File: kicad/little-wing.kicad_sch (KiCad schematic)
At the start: 132 parts, among them IC1 AP7335-WG-7, J1 nice!view, J10 rgb, J11 rows, J12 columns, J13 columns, J2 Battery, J3 trackball, J4 rotary, J5 trackball, J6 nice!view, J7 Battery, J8 rgb, J9 rows, SW1 Power, SW2 Reset, SW3 Reset, SW4 Power, U1 nice!nano v2, U2 PMW3610, U3 nice!nano v2

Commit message: Stashig the work
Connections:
- net MISO L renamed IRQ L
- net MISO R renamed IRQ R
- net MOSI L renamed SDIO L
- net MOSI R renamed SDIO R
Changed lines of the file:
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@@
 		)
 	)
-	(global_label "MISO R"
+	(global_label "IRQ R"
 		(shape input)
 		(at 35.56 121.92 180)
@@
 		)
 		(property "Intersheetrefs" "${INTERSHEET_REFS}"
-			(at 25.741 121.92 0)
+			(at 27.1319 121.92 0)
 			(effects
 				(font
@@
 		)
 	)
-	(global_label "MOSI L"
+	(global_label "SDIO L"
 		(shape input)
 		(at 36.83 69.85 180)
@@
 		)
 		(property "Intersheetrefs" "${INTERSHEET_REFS}"
-			(at 27.2529 69.85 0)
+			(at 27.4343 69.85 0)
 			(effects
 				(font
@@
 		)
 	)
-	(global_label "MOSI R"
+	(global_label "SDIO R"
 		(shape input)
 		(at 36.83 154.94 180)
@@
 		)
 		(property "Intersheetrefs" "${INTERSHEET_REFS}"
-			(at 27.011 154.94 0)
+			(at 27.1924 154.94 0)
 			(effects
 				(font
@@
 		)
 	)
-	(global_label "MOSI L"
+	(global_label "SDIO L"
 		(shape input)
 		(at 35.56 34.29 180)
@@
 		)
 		(property "Intersheetrefs" "${INTERSHEET_REFS}"
-			(at 25.9829 34.29 0)
-			(effects
-				(font
-					(size 1.27 1.27)
-				)
-				(justify right)
-				(hide yes)
-			)
-		)
-	)
-	(global_label "MISO L"
+			(at 26.1643 34.29 0)
+			(effects
+				(font
+					(size 1.27 1.27)
+				)
+				(justify right)
+				(hide yes)
+			)
+		)
+	)
+	(global_label "IRQ L"
 		(shape input)
 		(at 35.56 36.83 180)
@@
 		)
 		(property "Intersheetrefs" "${INTERSHEET_REFS}"
-			(at 25.9829 36.83 0)
+			(at 27.3738 36.83 0)
 			(effects
 				(font
@@
 		)
 	)
-	(global_label "MOSI R"
+	(global_label "SDIO R"
 		(shape input)
 		(at 67.31 152.4 180)
@@
 		)
 		(property "Intersheetrefs" "${INTERSHEET_REFS}"
-			(at 57.491 152.4 0)
+			(at 57.6724 152.4 0)
 			(effects
 				(font
@@
 		)
 	)
-	(global_label "MOSI R"
+	(global_label "SDIO R"
 		(shape input)
 		(at 35.56 119.38 180)
@@
 		)
 		(property "Intersheetrefs" "${INTERSHEET_REFS}"
-			(at 25.741 119.38 0)
+			(at 25.9224 119.38 0)
 			(effects
 				(font
@@
 		)
 	)
-	(global_label "MOSI L"
+	(global_label "SDIO L"
 		(shape input)
 		(at 62.23 64.77 180)
@@
 		)
 		(property "Intersheetrefs" "${INTERSHEET_REFS}"
-			(at 52.6529 64.77 0)
+			(at 52.8343 64.77 0)
 			(effects
 				(font
@@
 		)
 	)
-	(global_label "MISO R"
+	(global_label "IRQ R"
 		(shape input)
 		(at 36.83 160.02 180)
@@
 		)
 		(property "Intersheetrefs" "${INTERSHEET_REFS}"
-			(at 27.011 160.02 0)
+			(at 28.4019 160.02 0)
 			(effects
 				(font
@@
 		)
 	)
-	(global_label "MISO L"
+	(global_label "IRQ L"
 		(shape input)
 		(at 36.83 74.93 180)
@@
 		)
 		(property "Intersheetrefs" "${INTERSHEET_REFS}"
-			(at 27.2529 74.93 0)
-			(effects
-				(font
+			(at 28.6438 74.93 0)
+			(effects
+				(font

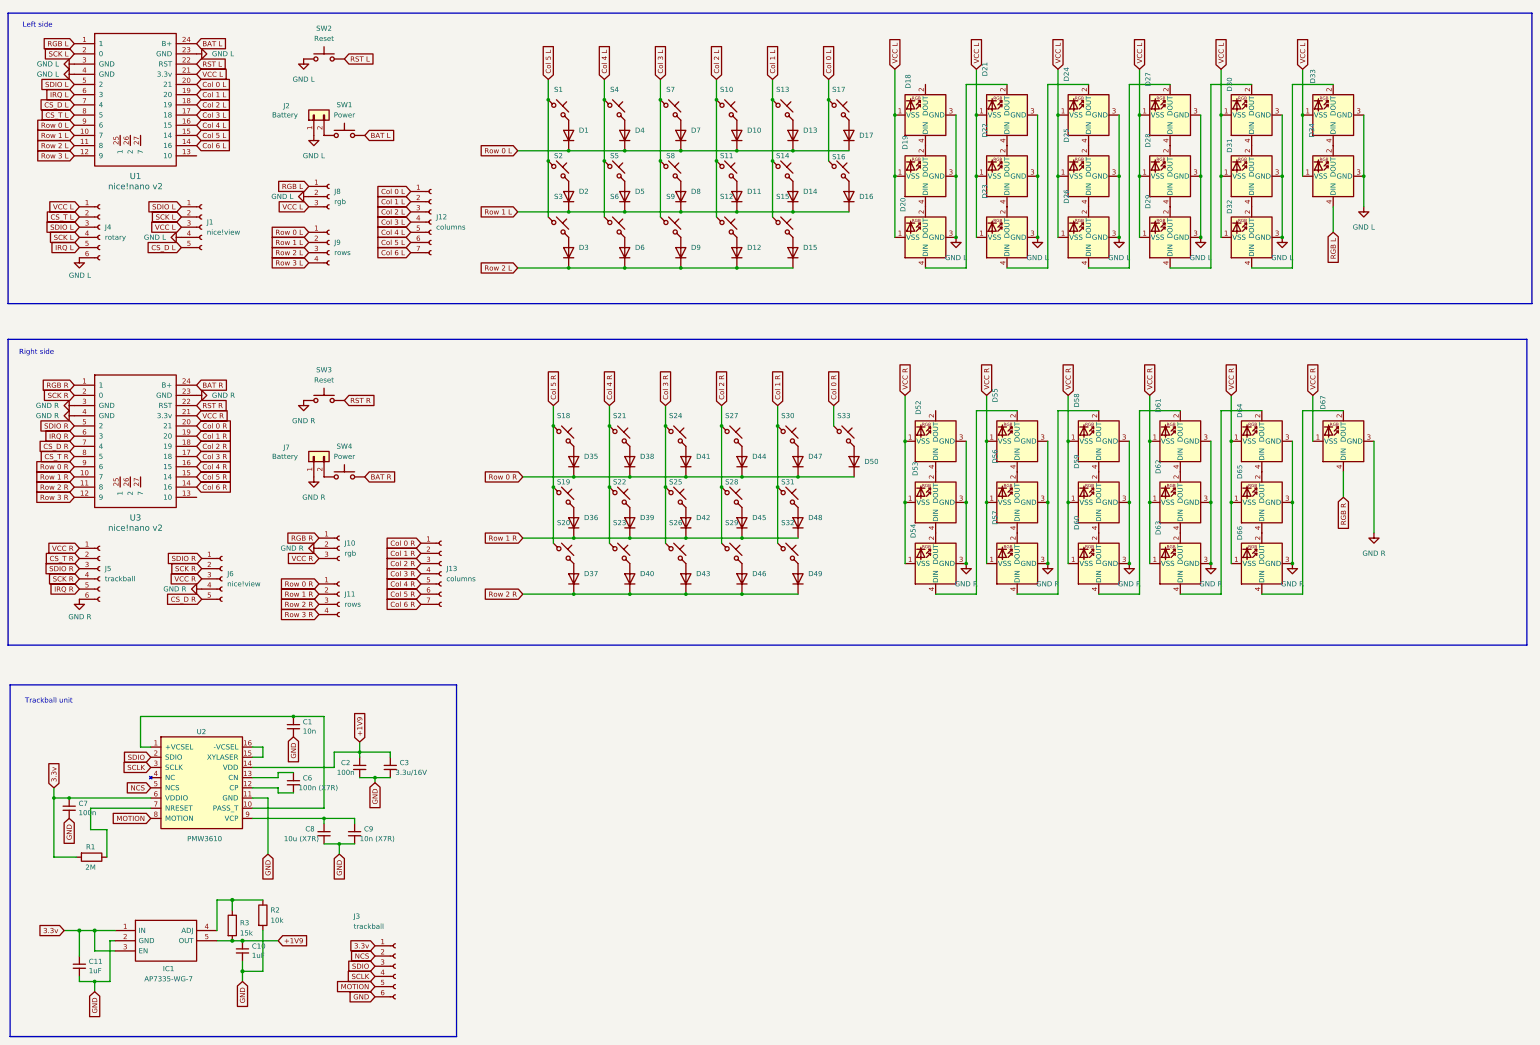
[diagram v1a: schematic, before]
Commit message: Reworking the schematics for a smaller power stepdown unit
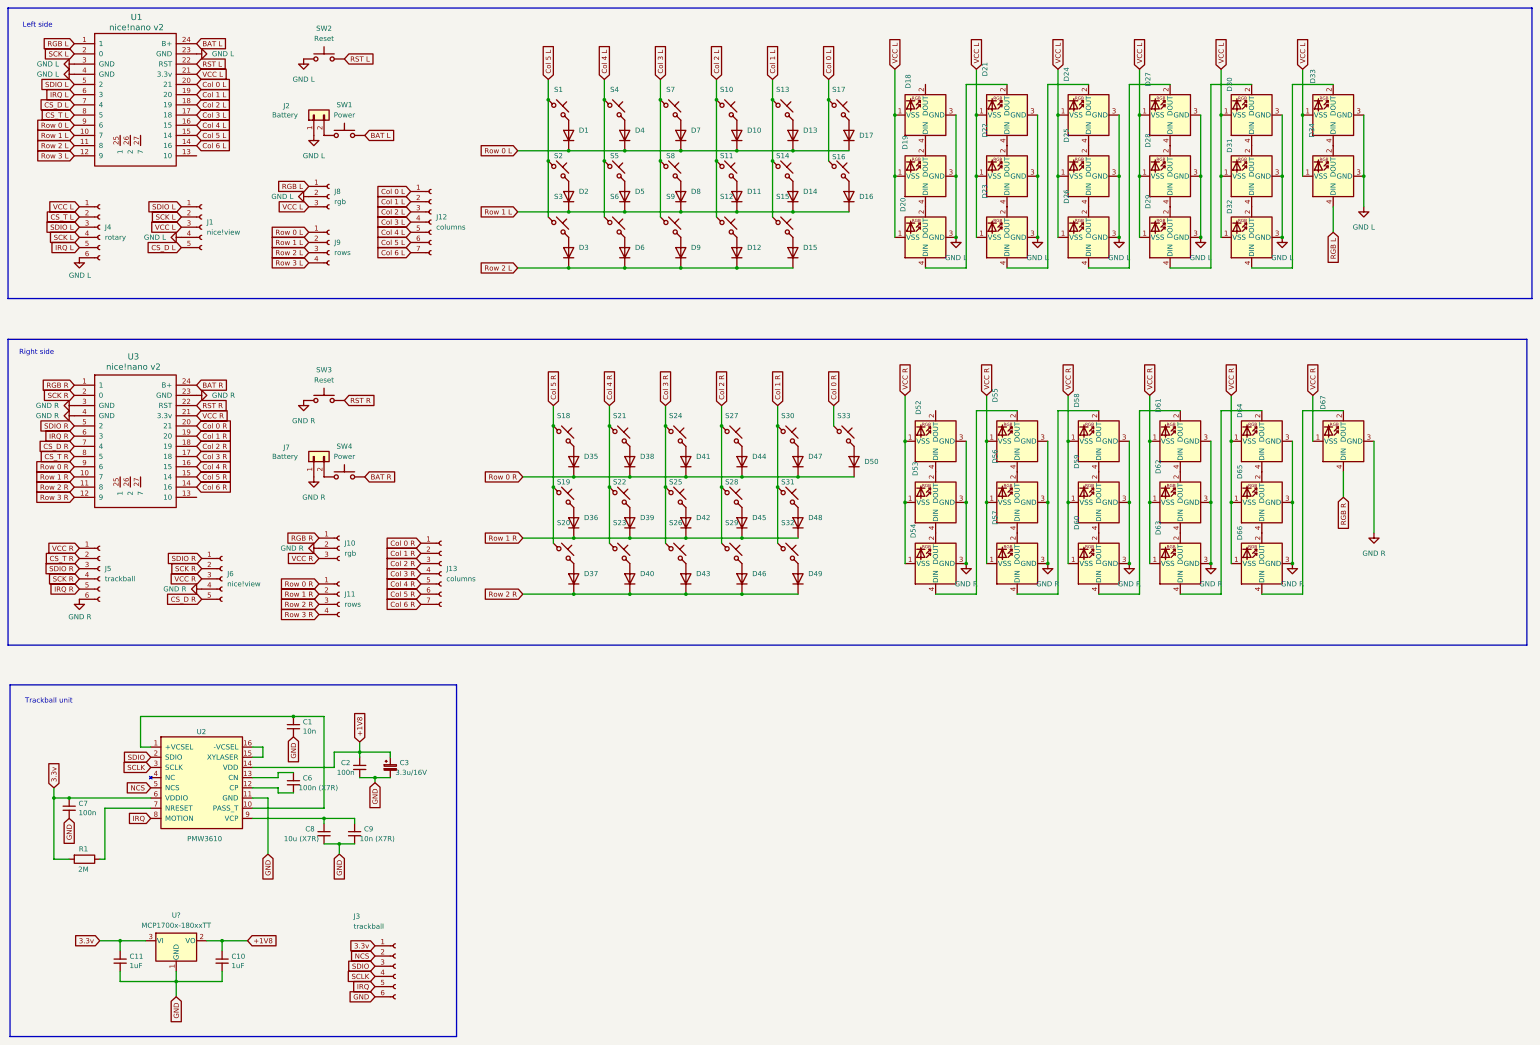
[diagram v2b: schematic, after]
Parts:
- removed IC1: AP7335-WG-7, Package_TO_SOT_SMD:SOT-23-5_HandSoldering, symbol AP7331-WG-7:AP7331-WG-7
- removed R2: 10k, Resistor_SMD:R_0603_1608Metric, symbol Device:R
- removed R3: 15k, Resistor_SMD:R_0603_1608Metric, symbol Device:R
- added U?: MCP1700x-180xxTT, Package_TO_SOT_SMD:SOT-23, symbol Regulator_Linear:MCP1700x-180xxTT
- C3: symbol Device:C_Small -> Device:C_Polarized_Small
- C6: value 100n (X7R) -> 100n (X7R)
- C8: value 10u (X7R) -> 10u (X7R)
- C9: value 10n (X7R) -> 10n (X7R)
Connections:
- net 3.3v: now also U?.3 (VI)
- net GND: now also U?.1 (GND)
- net +1V9 renamed +1V8
- net +1V8: now also U?.2 (VO)
- net MOTION renamed IRQ
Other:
- moved on the sheet: C10, C11, R1
